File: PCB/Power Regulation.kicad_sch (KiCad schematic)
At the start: 11 parts, among them U1 OPA569DWP

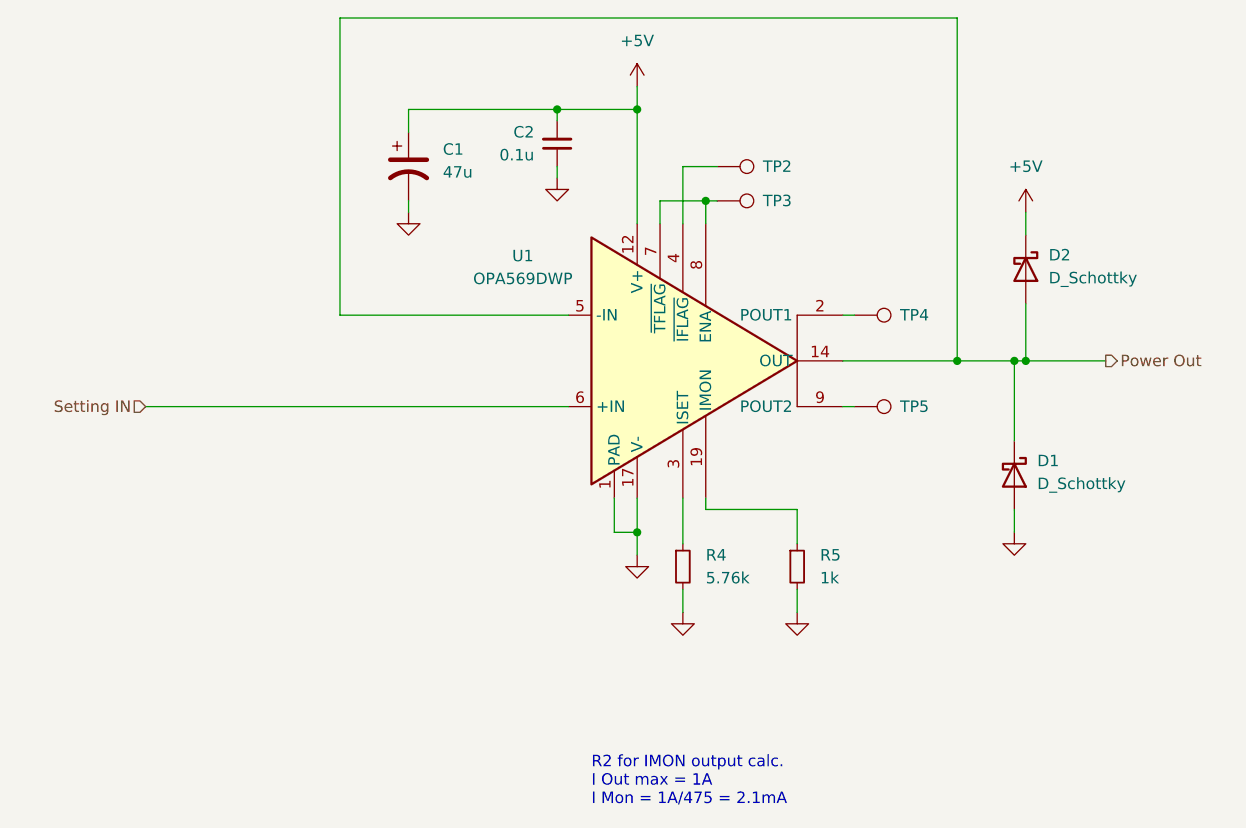
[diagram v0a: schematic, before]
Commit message: Added FUSB302B and associated circuitry.
Added FUSB302B, along with USB-C Connector and LDO.  The LDO is
needed to power the FUSB302B from the cable.

Also added some debugging and convenience items such as a QWIIC
connector and some test points.
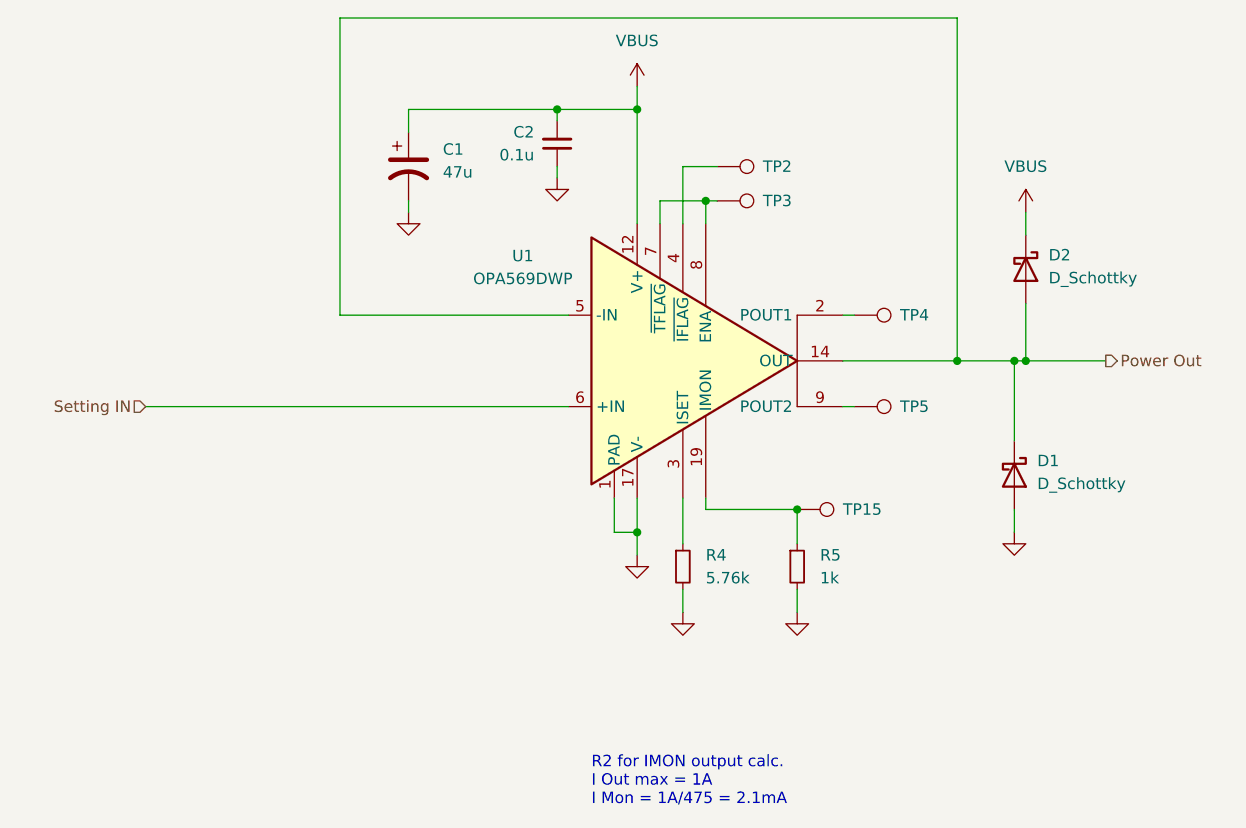
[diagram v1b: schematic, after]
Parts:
- added TP15: TestPoint, TestPoint:TestPoint_Keystone_5010-5014_Multipurpose, symbol Connector:TestPoint
- D1, D2: Mfg (none) -> Micro Commercial Co; P/N (none) -> SK310A-LTP
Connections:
- net at R5.1, U1.19 (IMON): now also TP15.1
- net +5V renamed VBUS
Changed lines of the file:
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@@
     (comment 1 "Client: None")
+  )
+  (junction (at 167.64 114.3) (diameter 0) (color 0 0 0 0)
   )
   (junction (at 149.86 69.85) (diameter 0) (color 0 0 0 0)
@@
       (effects (font (size 1.27 1.27)) hide)
     )
+    (property "Mfg" "Micro Commercial Co" (id 4) (at 193.04 87.63 0)
+      (effects (font (size 1.27 1.27)) hide)
+    )
+    (property "P/N" "SK310A-LTP" (id 5) (at 193.04 87.63 0)
+      (effects (font (size 1.27 1.27)) hide)
+    )
     (pin "1")
     (pin "2")
@@
       (effects (font (size 1.27 1.27)) hide)
     )
+    (property "Mfg" "Micro Commercial Co" (id 4) (at 191.77 110.49 0)
+      (effects (font (size 1.27 1.27)) hide)
+    )
+    (property "P/N" "SK310A-LTP" (id 5) (at 191.77 110.49 0)
+      (effects (font (size 1.27 1.27)) hide)
+    )
     (pin "1")
     (pin "2")
@@
     (pin "1")
     (pin "2")
+  )
+  (symbol (lib_id "power:VBUS") (at 193.04 81.28 0) (unit 1)
+    (in_bom yes) (on_board yes) (fields_autoplaced)
+    (property "Reference" "#PWR031" (id 0) (at 193.04 85.09 0)
+      (effects (font (size 1.27 1.27)) hide)
+    )
+    (property "Value" "VBUS" (id 1) (at 193.04 76.2 0))
+    (property "Footprint" "" (id 2) (at 193.04 81.28 0)
+      (effects (font (size 1.27 1.27)) hide)
+    )
+    (property "Datasheet" "" (id 3) (at 193.04 81.28 0)
+      (effects (font (size 1.27 1.27)) hide)
+    )
+    (pin "1")
   )
   (symbol (lib_id "Connector:TestPoint") (at 173.99 92.71 270) (unit 1)
@@
     (pin "2")
   )
-  (symbol (lib_id "power:+5V") (at 193.04 81.28 0) (unit 1)
-    (in_bom yes) (on_board yes) (fields_autoplaced)
-    (property "Reference" "#PWR012" (id 0) (at 193.04 85.09 0)
-      (effects (font (size 1.27 1.27)) hide)
-    )
-    (property "Value" "+5V" (id 1) (at 193.04 76.2 0))
-    (property "Footprint" "" (id 2) (at 193.04 81.28 0)
-      (effects (font (size 1.27 1.27)) hide)
-    )
-    (property "Datasheet" "" (id 3) (at 193.04 81.28 0)
+  (symbol (lib_id "Connector:TestPoint") (at 167.64 114.3 270) (unit 1)
+    (in_bom yes) (on_board yes) (fields_autoplaced)
+    (property "Reference" "TP15" (id 0) (at 172.72 114.2999 90)
+      (effects (font (size 1.27 1.27)) (justify left))
+    )
+    (property "Value" "TestPoint" (id 1) (at 172.72 115.5699 90)
+      (effects (font (size 1.27 1.27)) (justify left) hide)
+    )
+    (property "Footprint" "TestPoint:TestPoint_Keystone_5010-5014_Multipurpose" (id 2) (at 167.64 119.38 0)
+      (effects (font (size 1.27 1.27)) hide)
+    )
+    (property "Datasheet" "~" (id 3) (at 167.64 119.38 0)
       (effects (font (size 1.27 1.27)) hide)
     )
@@
     (pin "9")
   )
-  (symbol (lib_id "power:+5V") (at 149.86 67.31 0) (unit 1)
-    (in_bom yes) (on_board yes) (fields_autoplaced)
-    (property "Reference" "#PWR05" (id 0) (at 149.86 71.12 0)
-      (effects (font (size 1.27 1.27)) hide)
-    )
-    (property "Value" "+5V" (id 1) (at 149.86 62.23 0))
+  (symbol (lib_id "power:VBUS") (at 149.86 67.31 0) (unit 1)
+    (in_bom yes) (on_board yes) (fields_autoplaced)
+    (property "Reference" "#PWR030" (id 0) (at 149.86 71.12 0)
+      (effects (font (size 1.27 1.27)) hide)
+    )
+    (property "Value" "VBUS" (id 1) (at 149.86 62.23 0))
     (property "Footprint" "" (id 2) (at 149.86 67.31 0)
       (effects (font (size 1.27 1.27)) hide)

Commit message: Update to KiCAD v7, and finalize for V1 build
Updated to KiCAD v7, which touched many files.

Also made some changes to finalize board for prototype build.  Simplified the
circuit a bit to just something built and tested.
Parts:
- TP15, TP4, TP5: footprint TestPoint:TestPoint_Keystone_5010-5014_Multipurpose -> TestPoint:TestPoint_Keystone_5000-5004_Miniature
- TP2, TP3: footprint TestPoint:TestPoint_Keystone_5005-5009_Compact -> TestPoint:TestPoint_Keystone_5000-5004_Miniature
